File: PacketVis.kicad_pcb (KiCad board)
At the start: 2 copper layers, 59 x 44.5 mm, 36 parts, among them J1 USB_B_Micro, J2 Conn_01x04, SW1 SW_Push_Dual, SW2 SW_SPST, SW3 SW_SPST, U1 3.3V 1A, U2 74HC595, U3 ESP-WROOM-02D

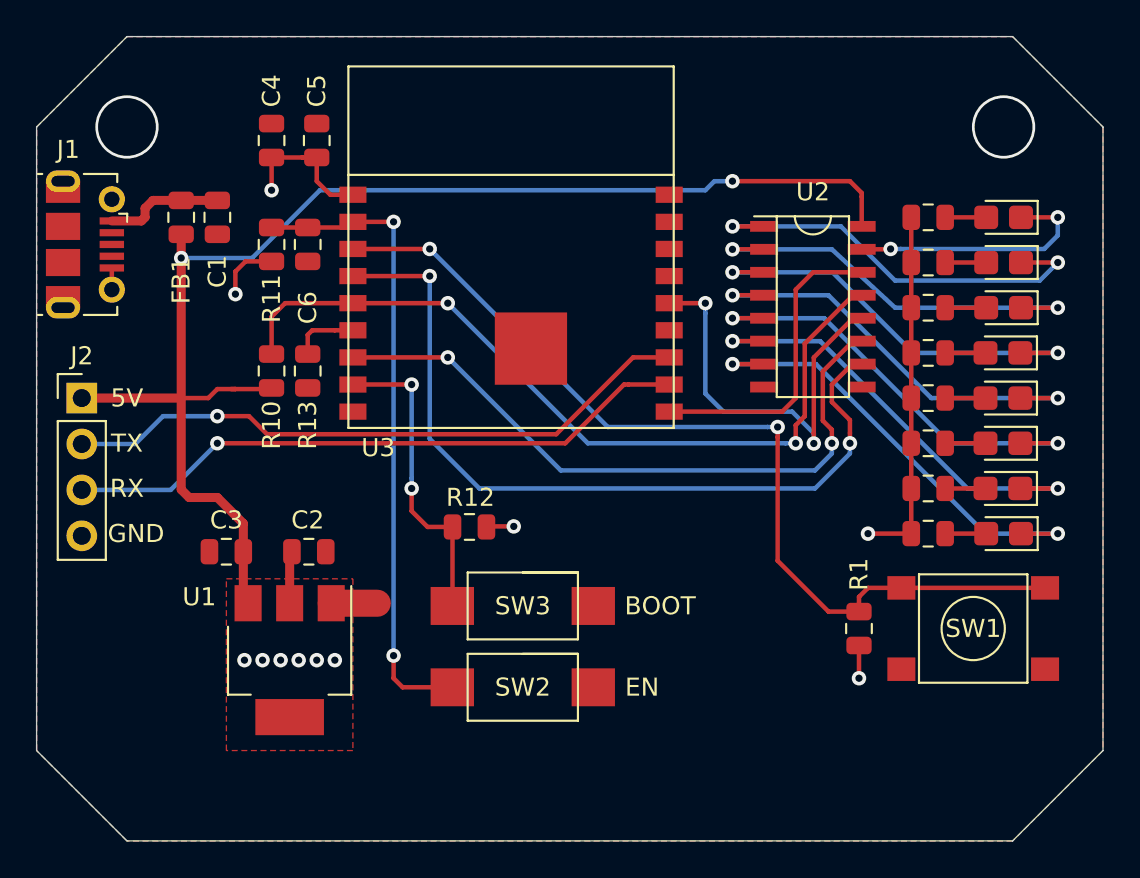
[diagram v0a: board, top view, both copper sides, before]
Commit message: Change Shift Register back to 3.3V
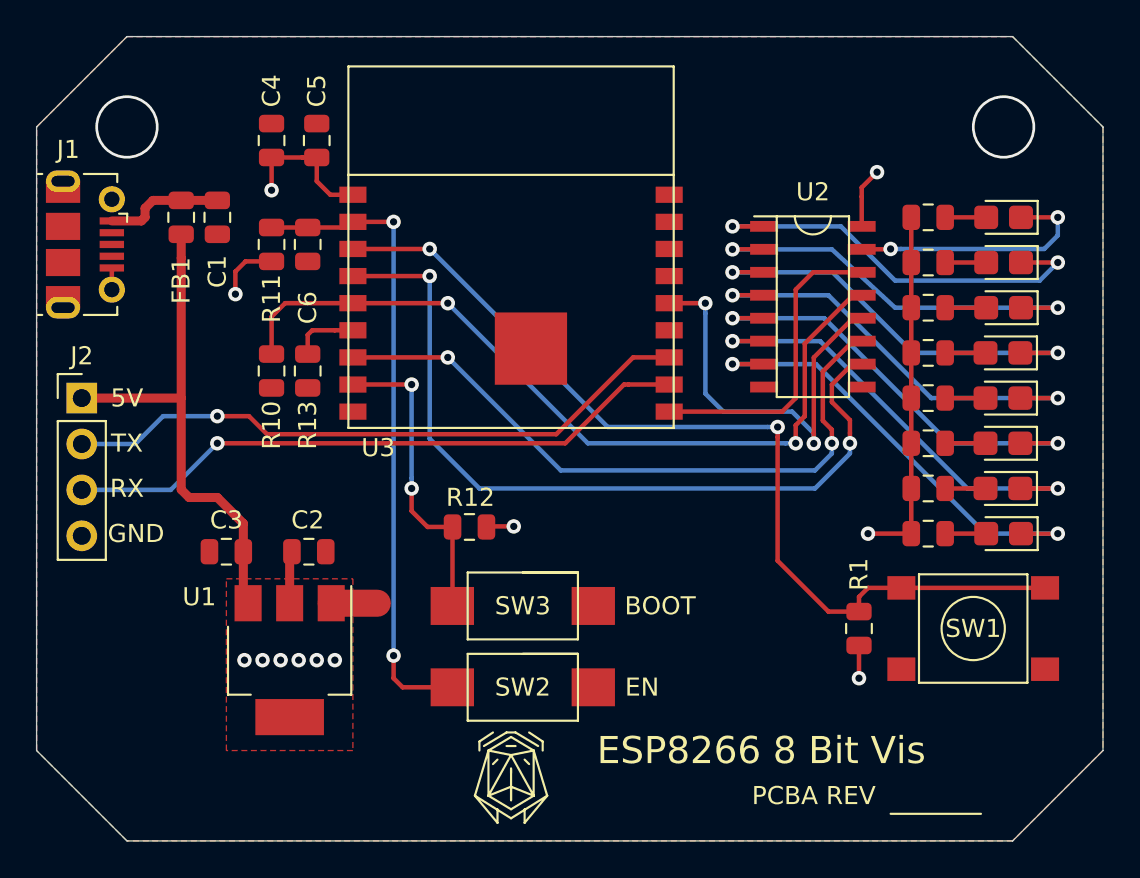
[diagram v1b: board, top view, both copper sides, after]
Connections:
- R10 pad 1: +5V -> GND
- U2 pad 16: +5V -> +3V3
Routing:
- net +5V: track 75.4 -> 28.4 mm, vias 2 -> 0
- net +3V3: track 37.6 -> 40.9 mm, vias 11 -> 12
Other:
- board text added: "A03"
- board text added: "ESP8266 8 Bit Vis"
- board text added: "Order Number"
- board text added: "PCBA REV"
- board text removed: "PacketVis REV: A02"
